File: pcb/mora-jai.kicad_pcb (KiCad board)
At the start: 2 copper layers, 150 x 150 mm, 72 parts, among them J1 Conn_01x02, J2 Conn_01x04, J3 Conn_01x02, J4 Conn_01x01, J5 Conn_01x03, SW1 SW_Push, SW10 SW_Push, SW11 SW_Push, SW12 SW_Push, SW13 SW_Push, SW14 SW_Push, SW15 SW_Push, SW16 SW_Push, SW2 SW_Push, SW3 SW_Push, SW4 SW_Push, SW5 SW_Push, SW6 SW_Push, SW7 SW_Push, SW8 SW_Push, SW9 SW_Push, U1 CD74HC4067M, U3 XIAO-ESP32-S3-SMD

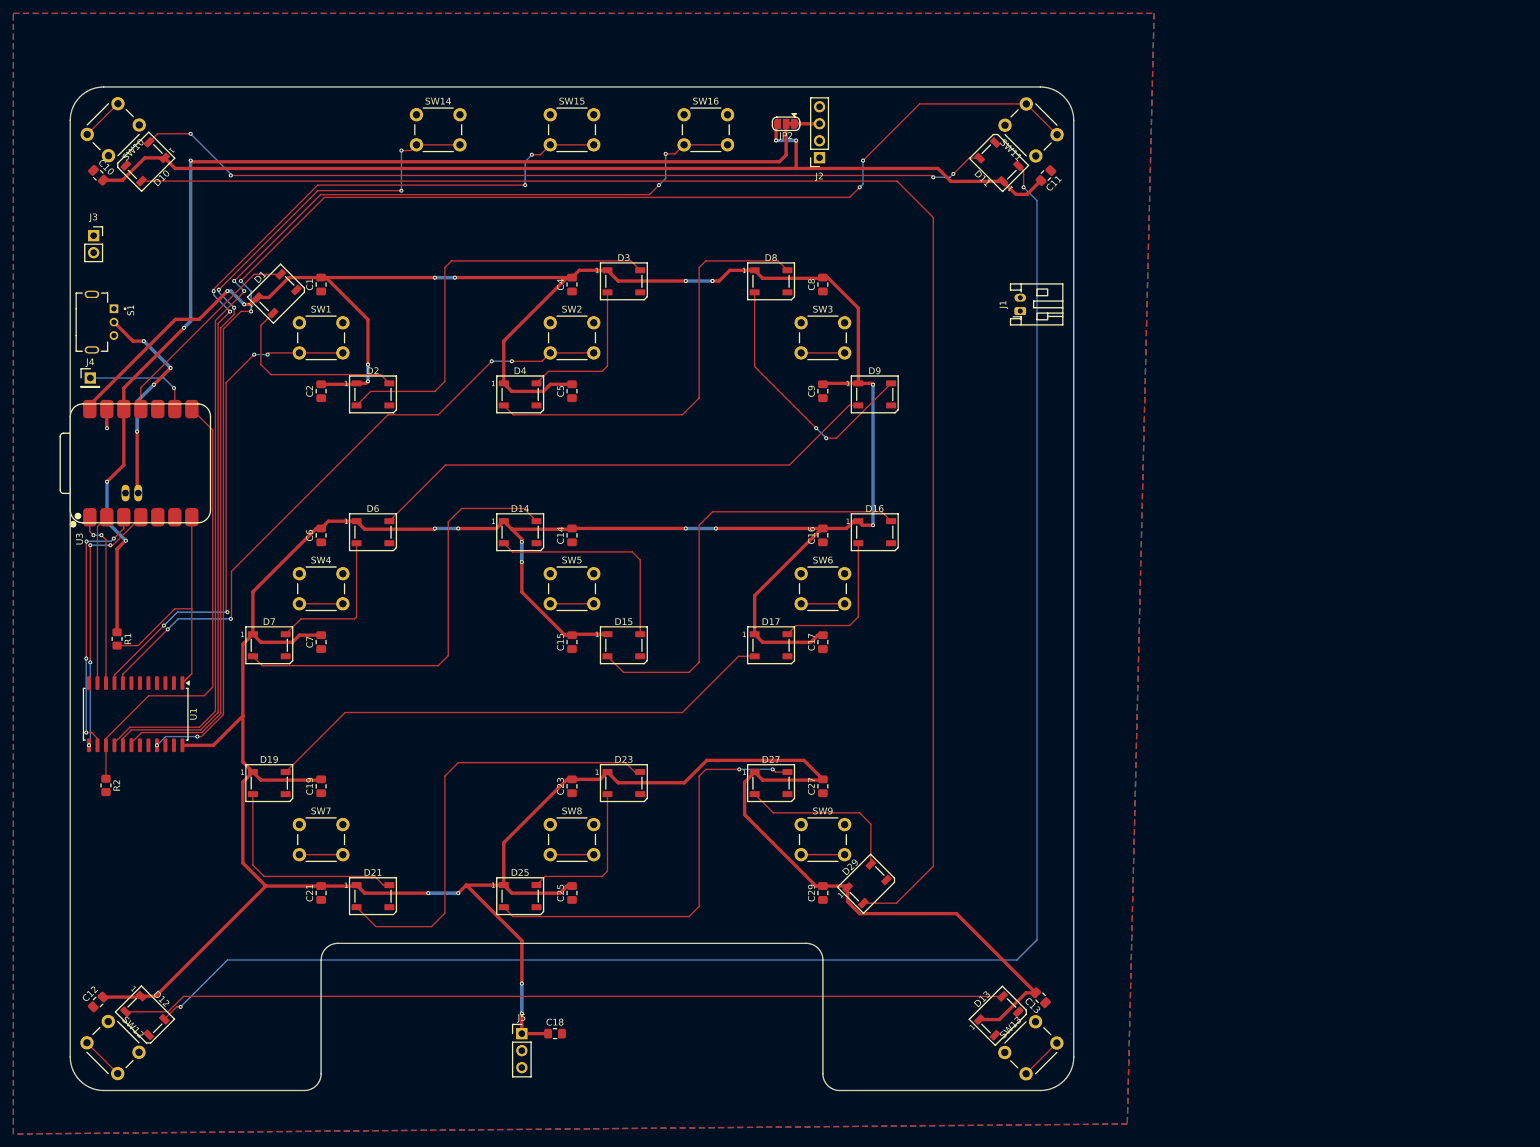
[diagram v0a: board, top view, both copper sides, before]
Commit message: DRC clean! all connections routed, now time for decoration
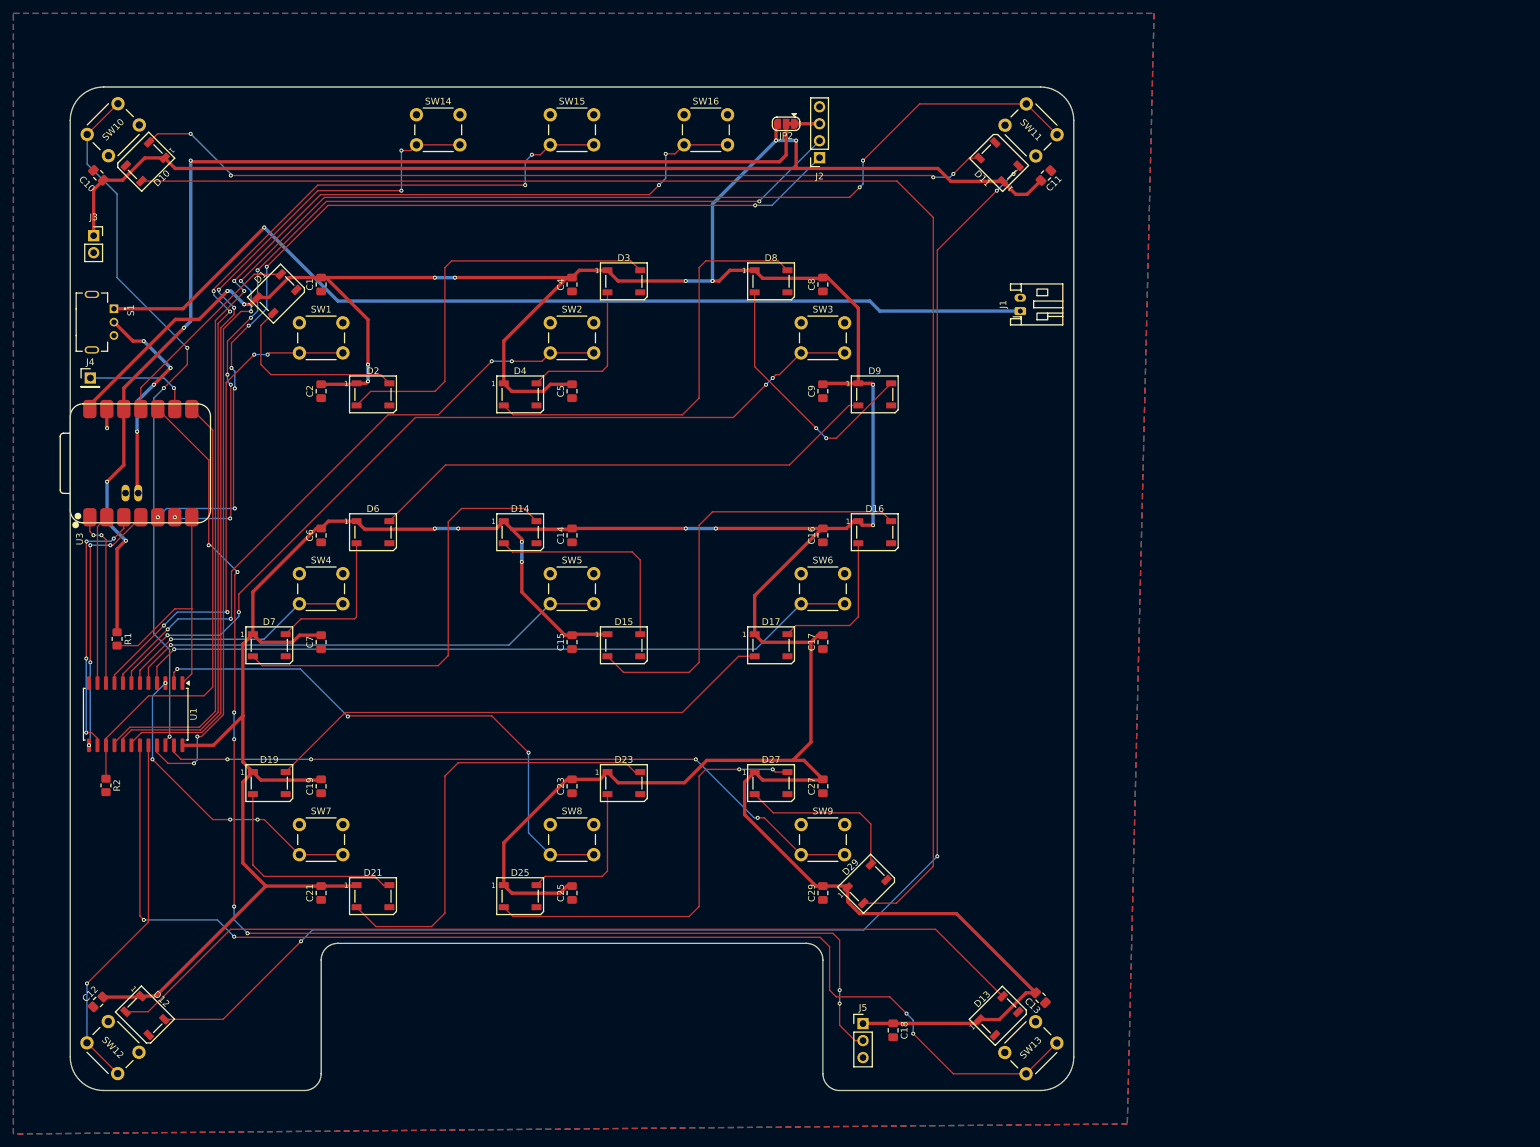
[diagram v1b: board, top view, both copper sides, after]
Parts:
- moved J5 51.0 mm to (144.5, 163.0)
- moved C18 50.5 mm to (149.0, 164.0), turned to -90 degrees
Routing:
- net MTR_CTRL: track 0.00 -> 190.6 mm, vias 0 -> 8
- net /SW_12: track 6.50 -> 179.2 mm, vias 0 -> 4
- net Net-(J1-Pin_1): track 0.00 -> 145.7 mm, vias 0 -> 1
- net SDA: track 0.00 -> 140.2 mm, vias 0 -> 7
- net SCL: track 0.00 -> 139.6 mm, vias 0 -> 7
- net /SW_2: track 6.50 -> 130.0 mm, vias 0 -> 4
- net /SW_5: track 6.50 -> 109.2 mm, vias 0 -> 1
- net /SW_8: track 6.50 -> 107.6 mm, vias 0 -> 4
- net /SW_9: track 6.50 -> 107.3 mm, vias 0 -> 3
- net /SW_7: track 6.50 -> 83.2 mm, vias 0 -> 3
- net /SW_4: track 6.50 -> 72.8 mm, vias 0 -> 1
- net /SW_11: track 6.50 -> 54.8 mm, vias 0 -> 1
- net /SW_6: track 6.50 -> 46.6 mm, vias 0 -> 4
- net /SW_3: track 6.50 -> 36.4 mm, vias 0 -> 1
- net Net-(D11-DOUT): track 252.2 -> 233.9 mm, vias 2 -> 4
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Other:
- board text removed: "TODO: Import and check sketches: - buttonRailsSketch.dxf - BoxTopCutouts.dxf"

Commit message: added utility silkscreen messages
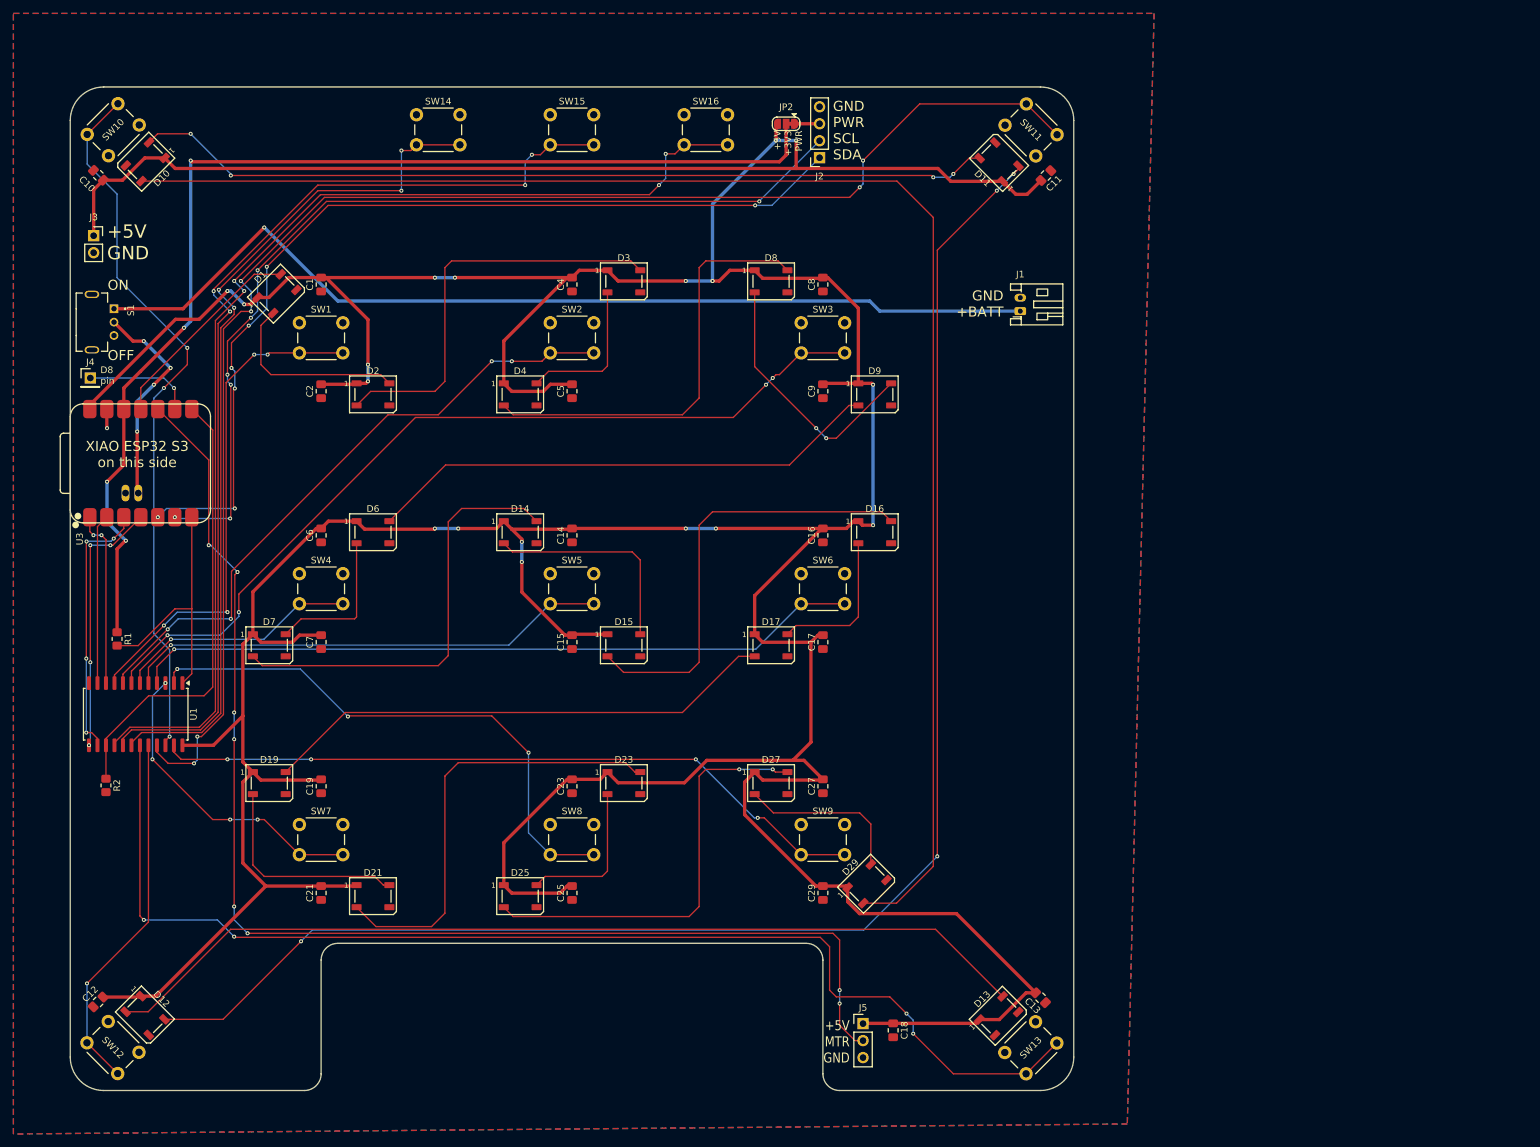
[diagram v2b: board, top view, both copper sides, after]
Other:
- board text added: "+5V +3V3 PWR"
- board text added: "+5V GND"
- board text added: "+5V MOTOR GND"
- board text added: "+5V MTR GND"
- board text added: "D8 pin"
- board text added: "GND +BATT"
- board text added: "GND PWR SCL SDA"
- board text added: "OFF"
- board text added: "ON"
- board text added: "XIAO ESP32 S3 on this side"
- board text removed: "TODO: Reposition battery connector according to sketch"
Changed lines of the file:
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@@
 		(tags "connector JST PH horizontal")
 		(property "Reference" "J1"
-			(at 1 -2.55 90)
+			(at 5.5 0 180)
 			(layer "F.SilkS")
 			(effects
@@
 		(tags "net tie solder jumper bridged")
 		(property "Reference" "JP2"
-			(at 0 -1.8 0)
+			(at 0 2.5 0)
 			(layer "F.SilkS")
 			(effects
@@
 		(layer "Edge.Cuts")
 	)
-	(gr_text "TODO: Reposition battery connector\naccording to sketch"
-		(at 178.5 55.5 0)
-		(layer "Cmts.User")
+	(gr_text "D8\npin"
+		(at 30.5 67.5 0)
+		(layer "F.SilkS")
+		(effects
+			(font
+				(size 1 1)
+			)
+			(justify left bottom)
+		)
+	)
+	(gr_text "+5V\n+3V3\nPWR"
+		(at 135.5 29.5 90)
+		(layer "F.SilkS")
+		(effects
+			(font
+				(size 1 1)
+			)
+			(justify right bottom)
+		)
+	)
+	(gr_text "+5V\nMTR\nGND"
+		(at 142.5 169 0)
+		(layer "F.SilkS")
+		(effects
+			(font
+				(size 1.5 1.25)
+			)
+			(justify right bottom)
+		)
+	)
+	(gr_text "ON"
+		(at 31.5855 53.5 0)
+		(layer "F.SilkS")
+		(effects
+			(font
+				(size 1.5 1.5)
+			)
+			(justify left bottom)
+		)
+	)
+	(gr_text "OFF"
+		(at 31.5855 64 0)
+		(layer "F.SilkS")
+		(effects
+			(font
+				(size 1.5 1.5)
+			)
+			(justify left bottom)
+		)
+	)
+	(gr_text "GND\nPWR\nSCL\nSDA"
+		(at 140 34 0)
+		(layer "F.SilkS")
+		(effects
+			(font
+				(size 1.5 1.5)
+			)
+			(justify left bottom)
+		)
+	)
+	(gr_text "XIAO ESP32 S3\non this side"
+		(at 36 80 0)
+		(layer "F.SilkS")
+		(effects
+			(font
+				(size 1.5 1.5)
+			)
+			(justify bottom)
+		)
+	)
+	(gr_text "GND\n+BATT"
+		(at 165.5 57.5 0)
+		(layer "F.SilkS")
+		(effects
+			(font
+				(size 1.5 1.5)
+			)
+			(justify right bottom)
+		)
+	)
+	(gr_text "+5V\nGND"
+		(at 31.5 49 0)
+		(layer "F.SilkS")
+		(effects
+			(font
+				(size 2 2)
+			)
+			(justify left bottom)
+		)
+	)
+	(gr_text "GND\nPWR\nSCL\nSDA"
+		(at 144.5 34.5 0)
+		(layer "B.SilkS")
+		(effects
+			(font
+				(size 1.5 1.5)
+			)
+			(justify left bottom mirror)
+		)
+	)
+	(gr_text "GND\n+BATT"
+		(at 167 57.5 0)
+		(layer "B.SilkS")
+		(effects
+			(font
+				(size 1.5 1.5)
+			)
+			(justify left bottom mirror)
+		)
+	)
+	(gr_text "+5V\nMOTOR\nGND"
+		(at 145.5 169 0)
+		(layer "B.SilkS")
+		(effects
+			(font
+				(size 1.5 1.5)
+			)
+			(justify right bottom mirror)
+		)
+	)
+	(gr_text "GND\n+BATT"
+		(at 37.5 82 90)
+		(layer "B.SilkS")
+		(effects
+			(font
+				(size 1.5 1.5)
+			)
+			(justify right bottom mirror)
+		)
+	)
+	(gr_text "+5V\nGND"
+		(at 37.5 49.5 0)
+		(layer "B.SilkS")
 		(effects
 			(font
 				(size 2 2)
-				(thickness 0.25)
 			)
-			(justify left)
+			(justify left bottom mirror)
 		)
 	)

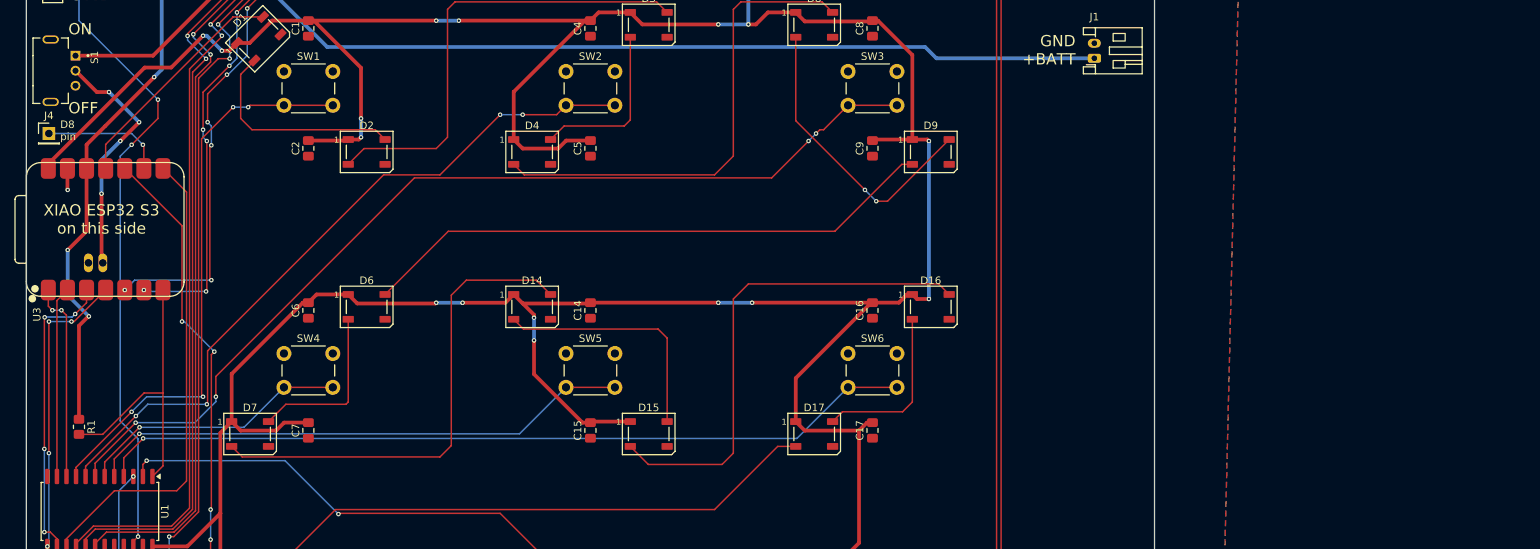
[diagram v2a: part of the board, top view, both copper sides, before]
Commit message: add mount holly and moon footprints and silkscreen
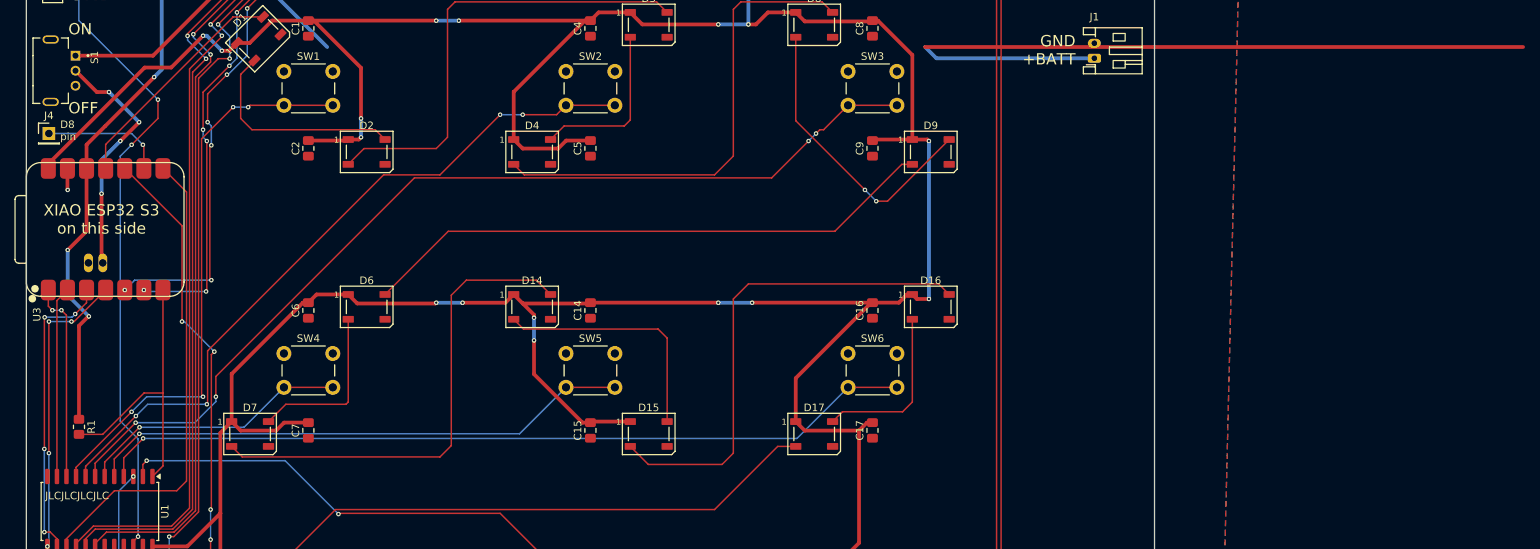
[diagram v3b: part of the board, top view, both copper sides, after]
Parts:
- added G***: LOGO, Mora_Jai_Parts:mount_holly, B.Cu at (102.5, 86.0)
- added G***: LOGO, Mora_Jai_Parts:moon_20mm, B.Cu at (162.0, 155.5)
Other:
- board text added: "JLCJLCJLCJLC"
- board text added: "Open Mora Jai Box"
- board text added: "Open Mora Jai Box PCB r1 Designed by: Alec Bargher"
- board text added: "To you, I grant that which, in life, I have given to no other: My esteem."

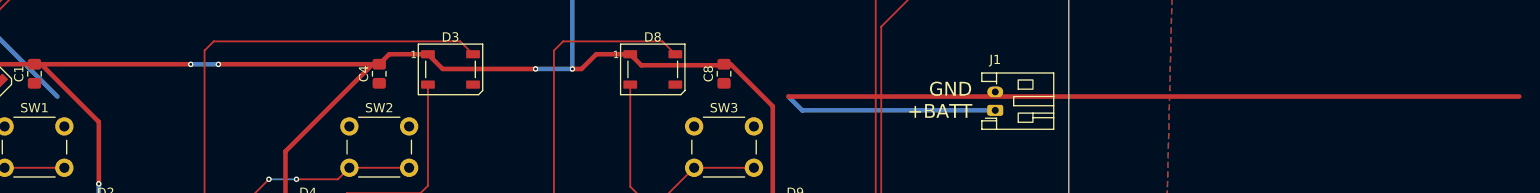
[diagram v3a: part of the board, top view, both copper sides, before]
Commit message: more silkscreen tweaks
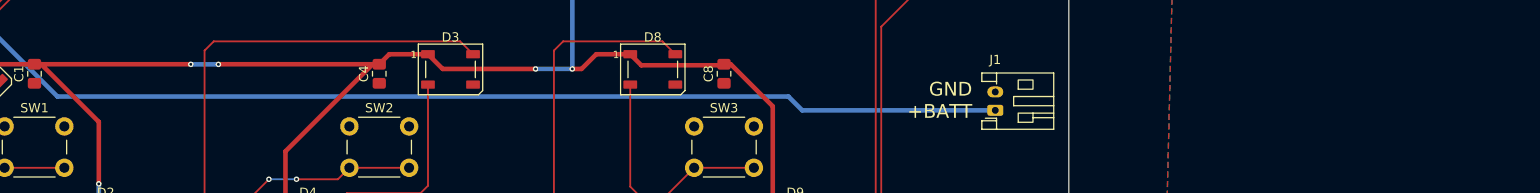
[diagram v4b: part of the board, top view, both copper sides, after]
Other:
- board text added: "Open Mora Jai Box PCB rev. 1 PCB+FW by: Alec Bargher CAD Model by: Eren Slifker Software by: Isaac Berman Emotional Support: shmoopy"
- board text removed: "Open Mora Jai Box PCB r1 Designed by: Alec Bargher"
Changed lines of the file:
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@@
 		)
 	)
-	(gr_text "Open Mora Jai Box PCB r1\nDesigned by: Alec Bargher"
-		(at 61 160 0)
+	(gr_text "Open Mora Jai Box PCB rev. 1\nPCB+FW by: Alec Bargher\nCAD Model by: Eren Slifker\nSoftware by: Isaac Berman\nEmotional Support: shmoopy"
+		(at 62 160.5 0)
 		(layer "B.SilkS")
 		(effects
@@
 		(net "Net-(J1-Pin_1)")
 	)
-	(segment
-		(start 145.5 55)
-		(end 225 55)
-		(width 0.5)
-		(layer "F.Cu")
-		(net "Net-(J1-Pin_1)")
-	)
 	(via
 		(at 55 44)
@@
 		(width 0.5)
 		(layer "B.Cu")
+		(net "Net-(J1-Pin_1)")
+	)
+	(segment
+		(start 145.5 55)
+		(end 66 55)
+		(width 0.5)
+		(layer "B.Cu")
